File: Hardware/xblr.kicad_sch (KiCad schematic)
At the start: 15 parts, among them J4 USB_C_Receptacle, J6 SWD, SW3 DPDT_Slide_SMD_7.2x3.5mm, U3 CH340C

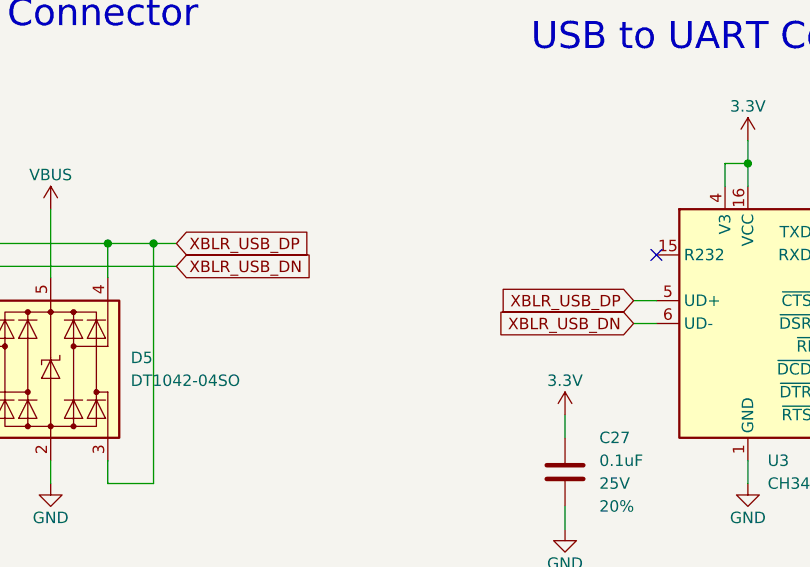
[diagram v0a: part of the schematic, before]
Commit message: Initial board layout
Board outline determined based off selected enclosure
Clusters of components placed and routed
Waiting for feedback before finishing routing
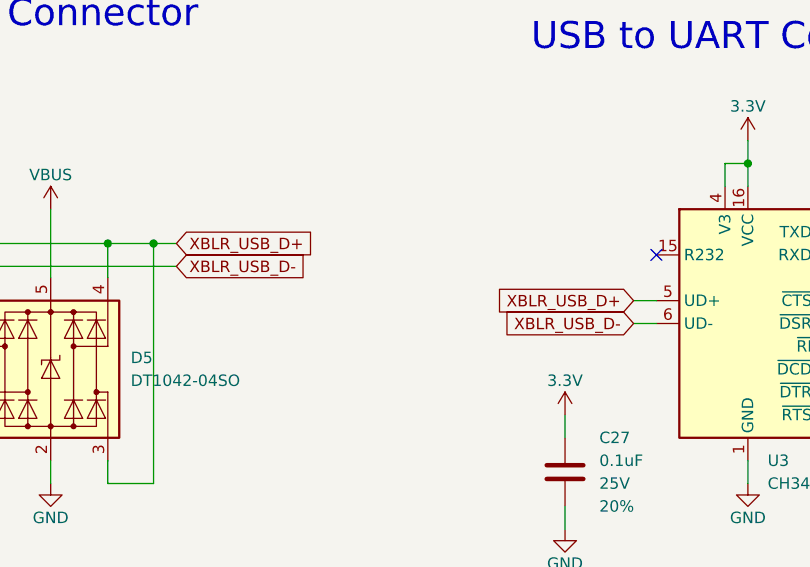
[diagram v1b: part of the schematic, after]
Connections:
- net XBLR_USB_DN renamed XBLR_USB_D-
- net XBLR_USB_DP renamed XBLR_USB_D+
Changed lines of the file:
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@@
 		)
 	)
-	(global_label "XBLR_USB_DN"
+	(global_label "XBLR_USB_D-"
 		(shape input)
 		(at 142.24 54.61 180)
@@
 		)
 		(property "Intersheetrefs" "${INTERSHEET_REFS}"
-			(at 126.1315 54.61 0)
-			(effects
-				(font
-					(size 1.27 1.27)
-				)
-				(justify right)
-				(hide yes)
-			)
-		)
-	)
-	(global_label "XBLR_USB_DN"
+			(at 125.8896 54.61 0)
+			(effects
+				(font
+					(size 1.27 1.27)
+				)
+				(justify right)
+				(hide yes)
+			)
+		)
+	)
+	(global_label "XBLR_USB_D-"
 		(shape input)
 		(at 91.44 48.26 0)
@@
 		)
 		(property "Intersheetrefs" "${INTERSHEET_REFS}"
-			(at 107.5485 48.26 0)
+			(at 107.7904 48.26 0)
 			(effects
 				(font
@@
 		)
 	)
-	(global_label "XBLR_USB_DP"
+	(global_label "XBLR_USB_D+"
 		(shape input)
 		(at 91.44 45.72 0)
@@
 		)
 		(property "Intersheetrefs" "${INTERSHEET_REFS}"
-			(at 107.488 45.72 0)
+			(at 107.7904 45.72 0)
 			(effects
 				(font
@@
 		)
 	)
-	(global_label "XBLR_USB_DP"
+	(global_label "XBLR_USB_D+"
 		(shape input)
 		(at 142.24 52.07 180)
@@
 		)
 		(property "Intersheetrefs" "${INTERSHEET_REFS}"
-			(at 126.192 52.07 0)
-			(effects
-				(font
+			(at 125.8896 52.07 0)
+			(effects
+				(font

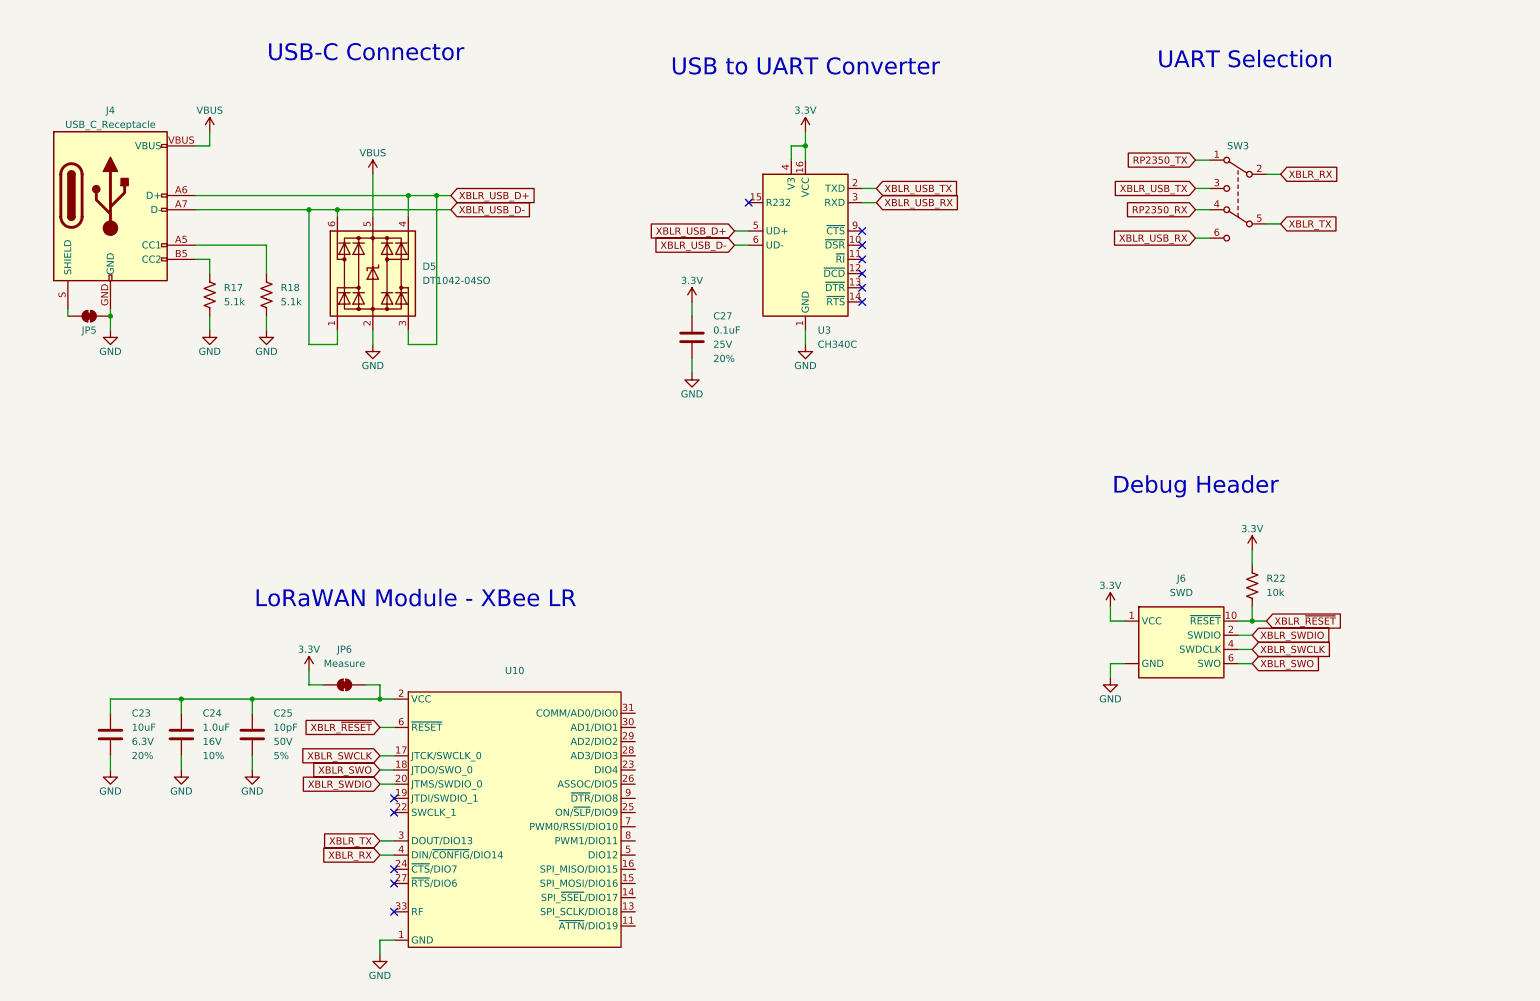
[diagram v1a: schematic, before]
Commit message: Finish connections and routing
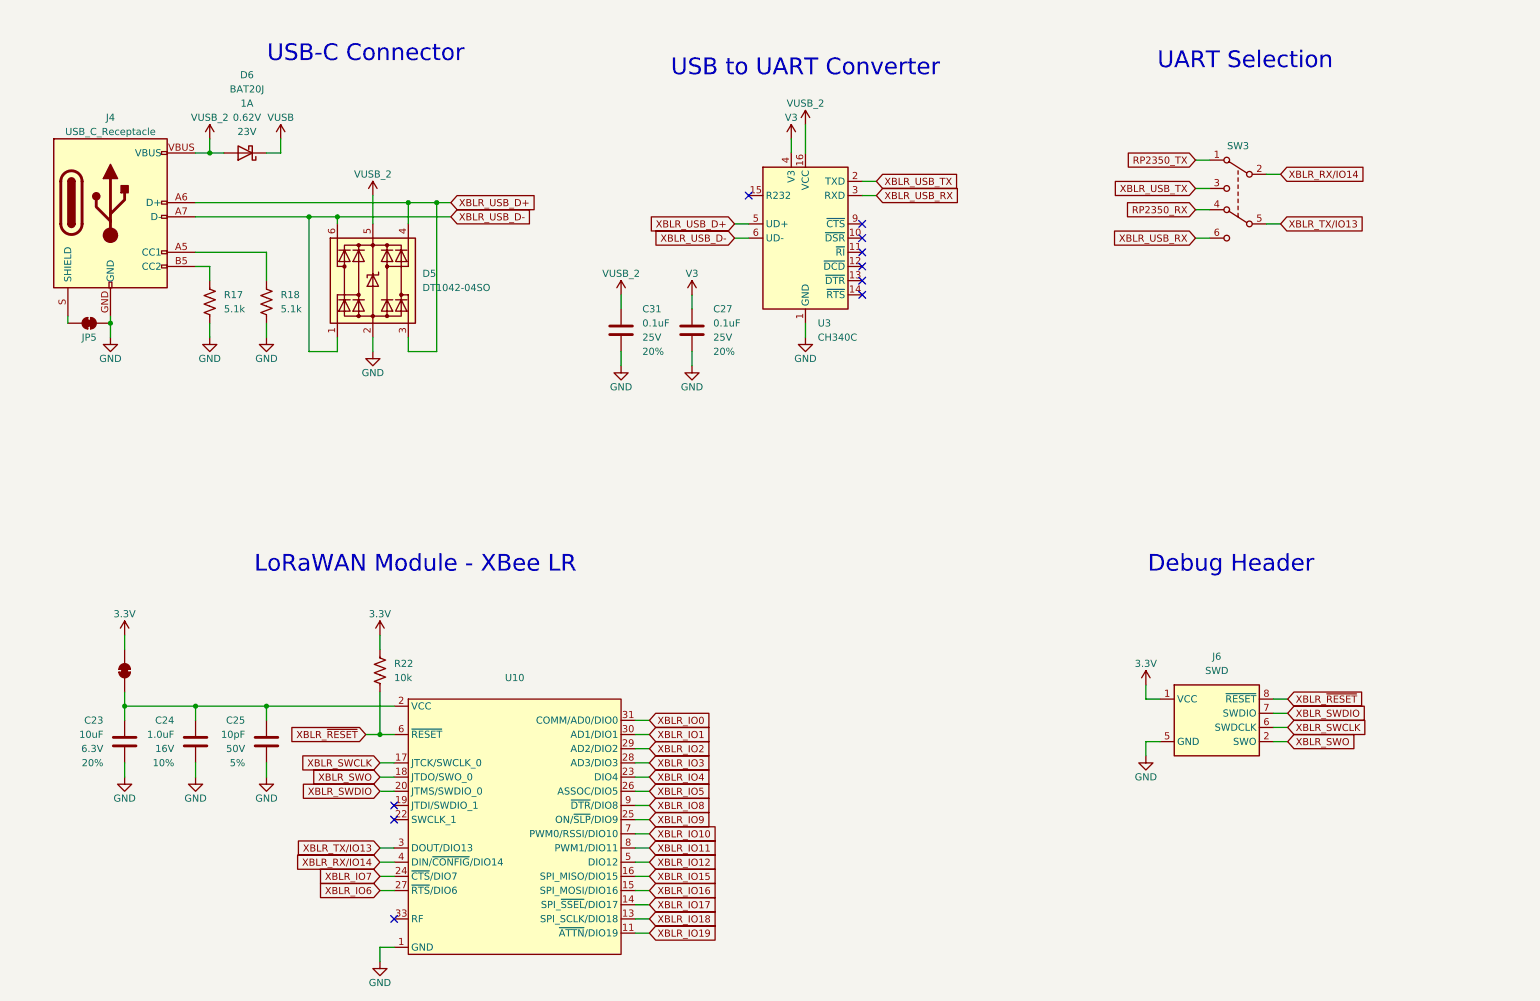
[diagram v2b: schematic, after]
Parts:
- added C31: 0.1uF, SparkFun-Capacitor:C_0603_1608Metric, symbol SparkFun-Capacitor:0.1uF_0603_25V_20%
- added D6: BAT20J, SparkFun-Semiconductor-Standard:SOD-323, symbol SparkFun-DiscreteSemi:D_Schottky_1A_23V_0.62V
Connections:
- net 3.3V: no longer C27.1, U3.16 (VCC), U3.4 (V3)
- net GND: now also C31.2; no longer J6.3 (GND), J6.9 (GND)
- net XBLR_SWCLK: now also J6.6 (SWDCLK); no longer J6.4 (SWDCLK)
- net XBLR_SWDIO: now also J6.7 (SWDIO); no longer J6.2 (SWDIO)
- net XBLR_SWO: now also J6.2 (SWO); no longer J6.6 (SWO)
- net XBLR_~{RESET}: now also J6.8 (~{RESET}); no longer J6.10 (~{RESET})
- net XBLR_IO19: now reaches U10.11 (~{ATTN}/DIO19)
- net XBLR_IO18: now reaches U10.13 (SPI_SCLK/DIO18)
- net XBLR_IO17: now reaches U10.14 (SPI_~{SSEL}/DIO17)
- net XBLR_IO16: now reaches U10.15 (SPI_MOSI/DIO16)
- net XBLR_IO15: now reaches U10.16 (SPI_MISO/DIO15)
- net XBLR_IO4: now reaches U10.23 (DIO4)
- net XBLR_IO7: now reaches U10.24 (~{CTS}/DIO7)
- net XBLR_IO9: now reaches U10.25 (ON/~{SLP}/DIO9)
- net XBLR_IO5: now reaches U10.26 (ASSOC/DIO5)
- net XBLR_IO6: now reaches U10.27 (~{RTS}/DIO6)
- net XBLR_IO3: now reaches U10.28 (AD3/DIO3)
- net XBLR_IO2: now reaches U10.29 (AD2/DIO2)
- net XBLR_IO1: now reaches U10.30 (AD1/DIO1)
- net XBLR_IO0: now reaches U10.31 (COMM/AD0/DIO0)
- net XBLR_IO12: now reaches U10.5 (DIO12)
- net XBLR_IO10: now reaches U10.7 (PWM0/RSSI/DIO10)
- net XBLR_IO11: now reaches U10.8 (PWM1/DIO11)
- net XBLR_IO8: now reaches U10.9 (~{DTR}/DIO8)
- net VBUS renamed VUSB_2
- net VUSB_2: now also U3.16 (VCC), C31.1, D6.A
- net XBLR_RX renamed XBLR_RX/IO14
- net XBLR_TX renamed XBLR_TX/IO13
- new net V3: C27.1, U3.4 (V3)
- new net VUSB: D6.C
- no-connect marks 12 -> 10
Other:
- moved on the sheet: C23, C24, C25, C27, D5, J4, JP5, R17, R18, U10, U3

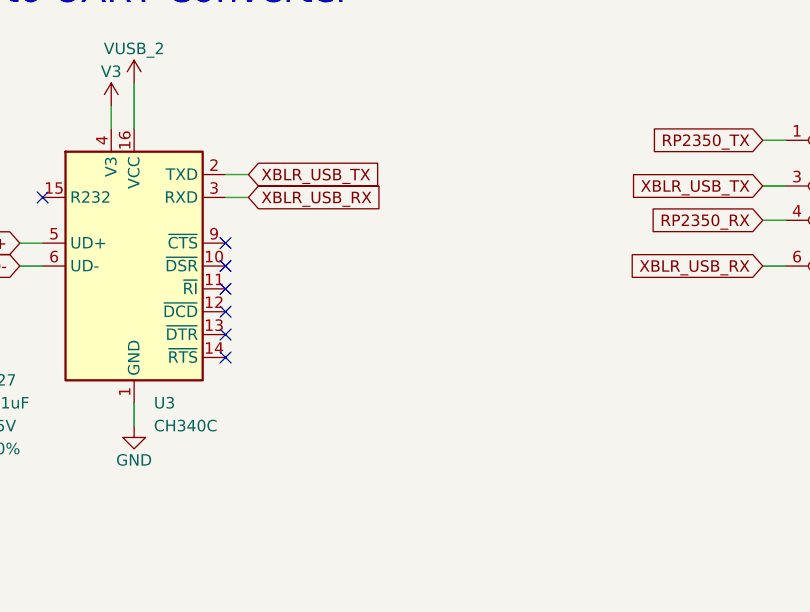
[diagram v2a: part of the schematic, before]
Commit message: Add level shifter to CH340 TX pin
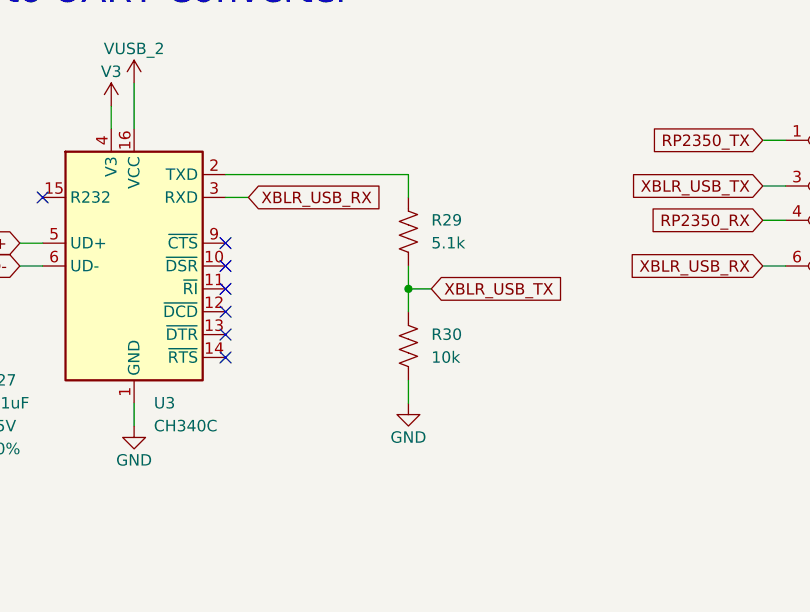
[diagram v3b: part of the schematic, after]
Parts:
- added R29: 5.1k, SparkFun-Resistor:R_0603_1608Metric, symbol SparkFun-Resistor:5.1k_0603
- added R30: 10k, SparkFun-Resistor:R_0603_1608Metric, symbol SparkFun-Resistor:10k_0603
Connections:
- net GND: now also R30.2
- net XBLR_USB_TX: now also R29.2, R30.1; no longer U3.2 (TXD)
- new net: R29.1, U3.2 (TXD)

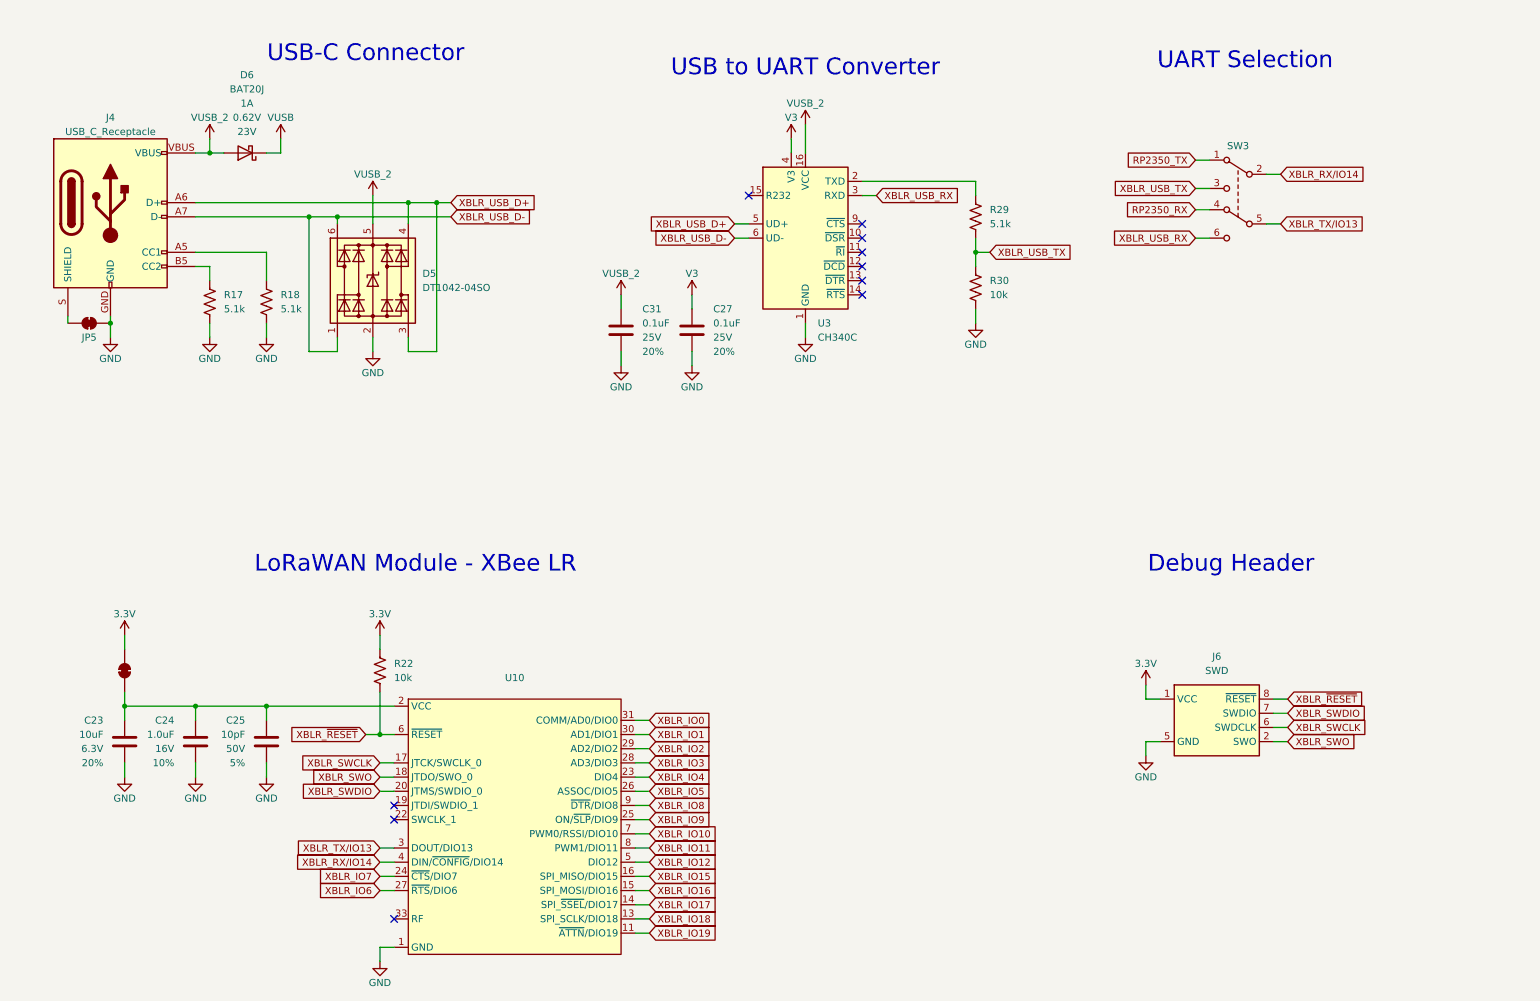
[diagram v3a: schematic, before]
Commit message: Clean up schematic
Add lines between regions
Add instruction text to all jumpers
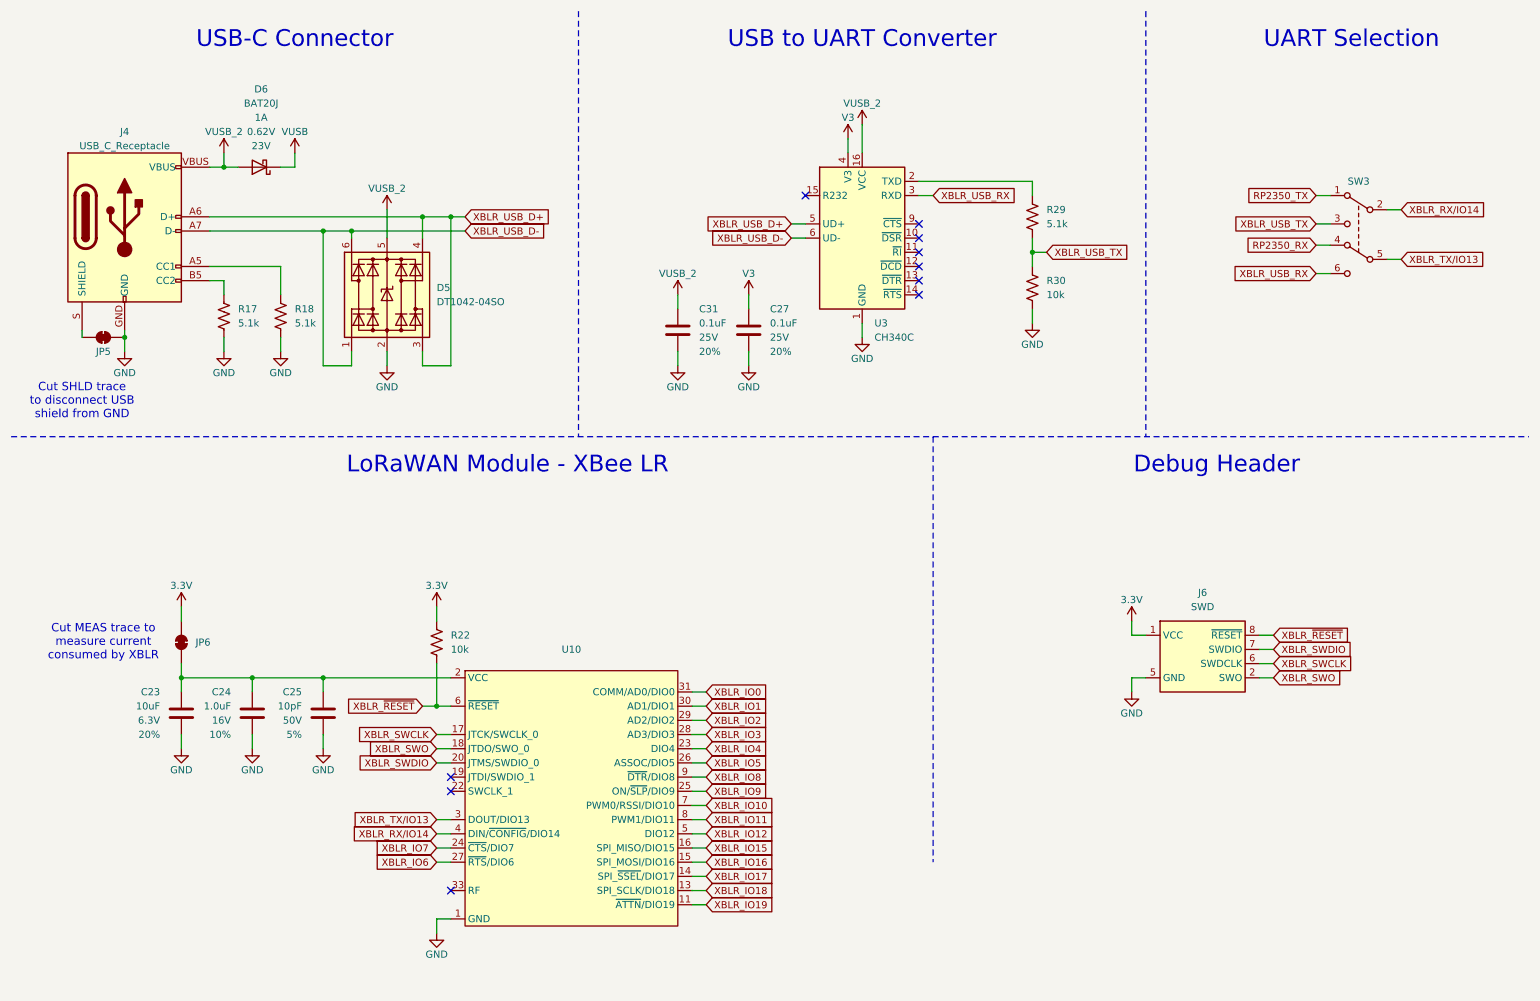
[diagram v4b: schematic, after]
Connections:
- net 3.3V: now also JP6.2 (B); no longer JP6.1 (A)
- net at C23.1, C24.1, C25.1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: now also JP6.1 (A); no longer JP6.2 (B)
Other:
- note added: "Cut MEAS trace to measure current consumed by XBLR"
- note added: "Cut SHLD trace to disconnect USB shield from GND"
- moved on the sheet: C23, C24, C25, C27, C31, D5, D6, J4, J6, JP5, R17, R18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
